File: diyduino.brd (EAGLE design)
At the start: 57.1 x 53.3 mm, 22 parts, among them Q2 16MHz

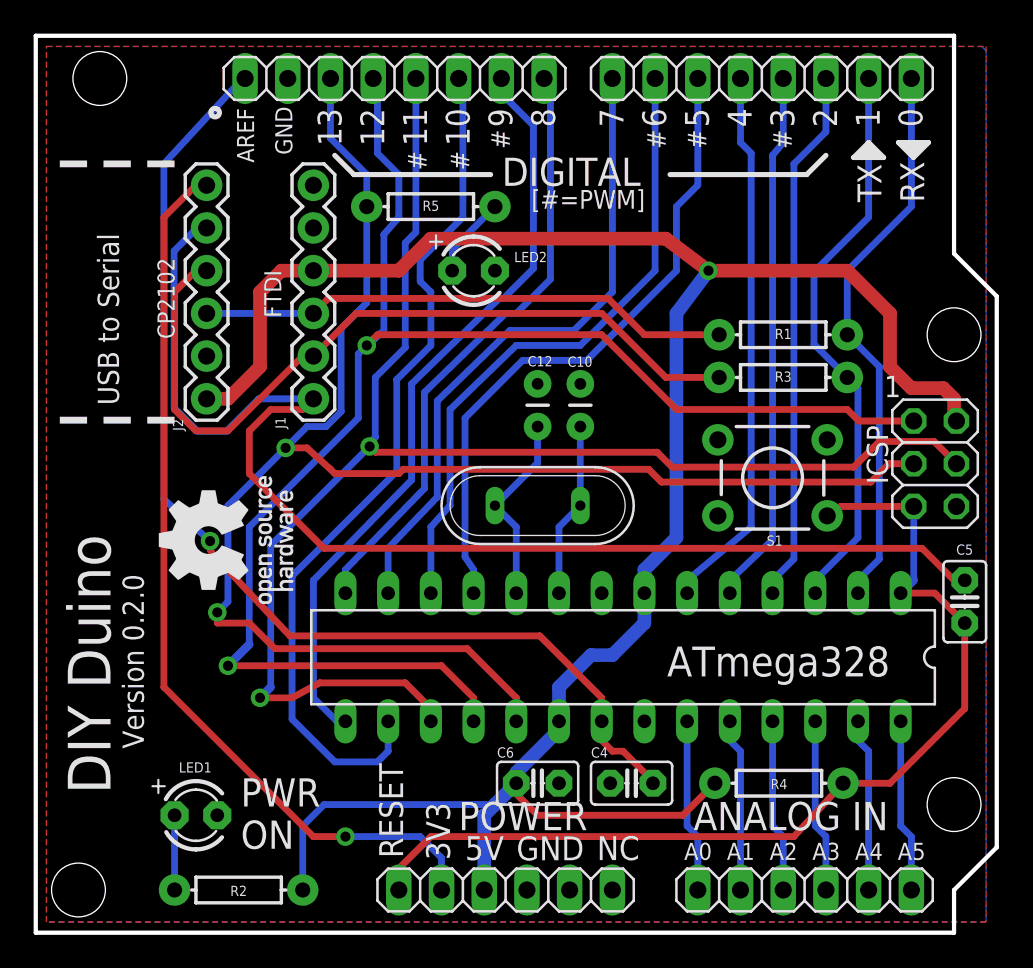
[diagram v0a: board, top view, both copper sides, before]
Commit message: 0.3.0 changes, fixed CH340 pinout, changed crystal to resonator
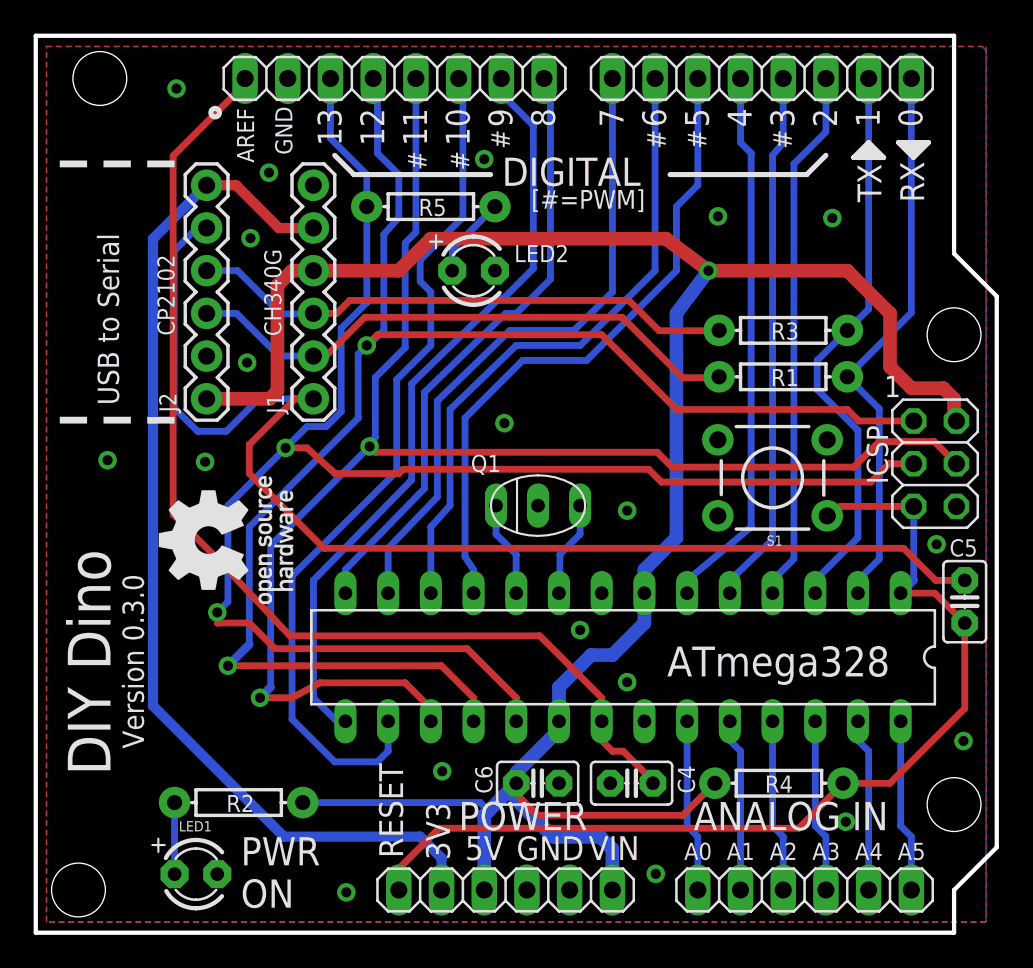
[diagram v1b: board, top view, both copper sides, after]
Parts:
- removed C10, C12: 22pF, SparkFun-Capacitors:CAP-PTH-2.54
- removed Q2: 16MHz, special:QS
- added Q1: (no value), murata-resonators:CSTLS_X
- moved R2 5.20 mm to (23.5, 7.74)
- moved LED1 3.50 mm to (21.0, 3.48)
- moved R3 2.80 mm to (55.9, 35.8)
- moved R1 2.50 mm to (55.9, 33.1)
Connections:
- removed net VIN: POWER.6
- net +3V3: now also J1.5
- net +5V: now also POWER.6
- net GND: now also Q1.2; no longer C10.1, C12.1, J1.5
- net M8RXD: now also J1.2; no longer J1.3
- net M8TXD: now also J1.3; no longer J1.2
- net XTAL1: now also Q1.3; no longer C10.2, Q2.2
- net XTAL2: now also Q1.1; no longer C12.2, Q2.1
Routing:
- net M8TXD: track 46.8 -> 32.6 mm
- net +3V3: track 53.9 -> 63.1 mm, vias 1 -> 0
- net +5V: track 130.5 -> 137.4 mm
- net XTAL2: track 11.5 -> 5.71 mm
- net XTAL1: track 10.4 -> 5.73 mm
- net M8RXD: track 31.7 -> 34.0 mm
- net AREF: track 65.5 -> 65.0 mm, vias 1 -> 0
- net GND: vias 0 -> 19
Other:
- board text added: "/Users/chris/Downloads/cc-by-sa-bw.bmp"
- board text added: "CH340G"
- board text added: "DIY Dino"
- board text added: "VIN"
- board text added: "Version 0.3.0"
- board text removed: "C10"
- board text removed: "C12"
- board text removed: "DIY Duino"
- board text removed: "FTDI"
- board text removed: "NC"
- board text removed: "Version 0.2.0"

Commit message: adding dinosaur!
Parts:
- moved R2 42.9 mm to (55.9, 35.8), turned to 0 degrees
- moved R3 42.9 mm to (23.5, 7.74), turned to 180 degrees
- moved R4 40.1 mm to (34.9, 43.2), turned to 0 degrees
- moved R5 40.1 mm to (55.6, 8.89), turned to 180 degrees
- renumbered C4 to C3, C5 to C1, C6 to C2
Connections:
- net +5V: now also R3.P$1, R5.P$2; no longer R2.P$1, R4.P$2
- net IO1: now also R2.P$2; no longer R3.P$2
- net M8TXD: now also R2.P$1; no longer R3.P$1
- net N$1: now also R4.P$2; no longer R5.P$2
- net N$2: now also R3.P$2; no longer R2.P$2
- net RESET: now also R5.P$1; no longer R4.P$1
- net SCK: now also R4.P$1; no longer R5.P$1
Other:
- board text added: "C1"
- board text added: "C2"
- board text added: "C3"
- board text removed: "C4"
- board text removed: "C5"
- board text removed: "C6"
